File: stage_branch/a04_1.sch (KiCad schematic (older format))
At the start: 38 parts, among them U4001 74HC02, U4002 74HC27, U4003 74LVC07, U4004 74HC27, U4005 74HC02, U4006 74HC02, U4007 74HC04, U4008 74HC04, U4009 74HC27, U4010 74HC4002, U4011 74HC02, U4012 74HC02, U4013 74HC02, U4014 74HC4002, U4015 74HC27, U4016 74HC02, U4017 74HC04, U4018 74HC02, U4019 74HC02, U4020 74HC27, U4021 74HC02, U4022 74HC4002, U4023 74LVC07, U4024 74HC02, U4025 74HC04, U4026 74HC27, U4027 74HC4002, U4028 74HC4002, U4029 74LVC07, U4030 74HC02, U4058 74HC04

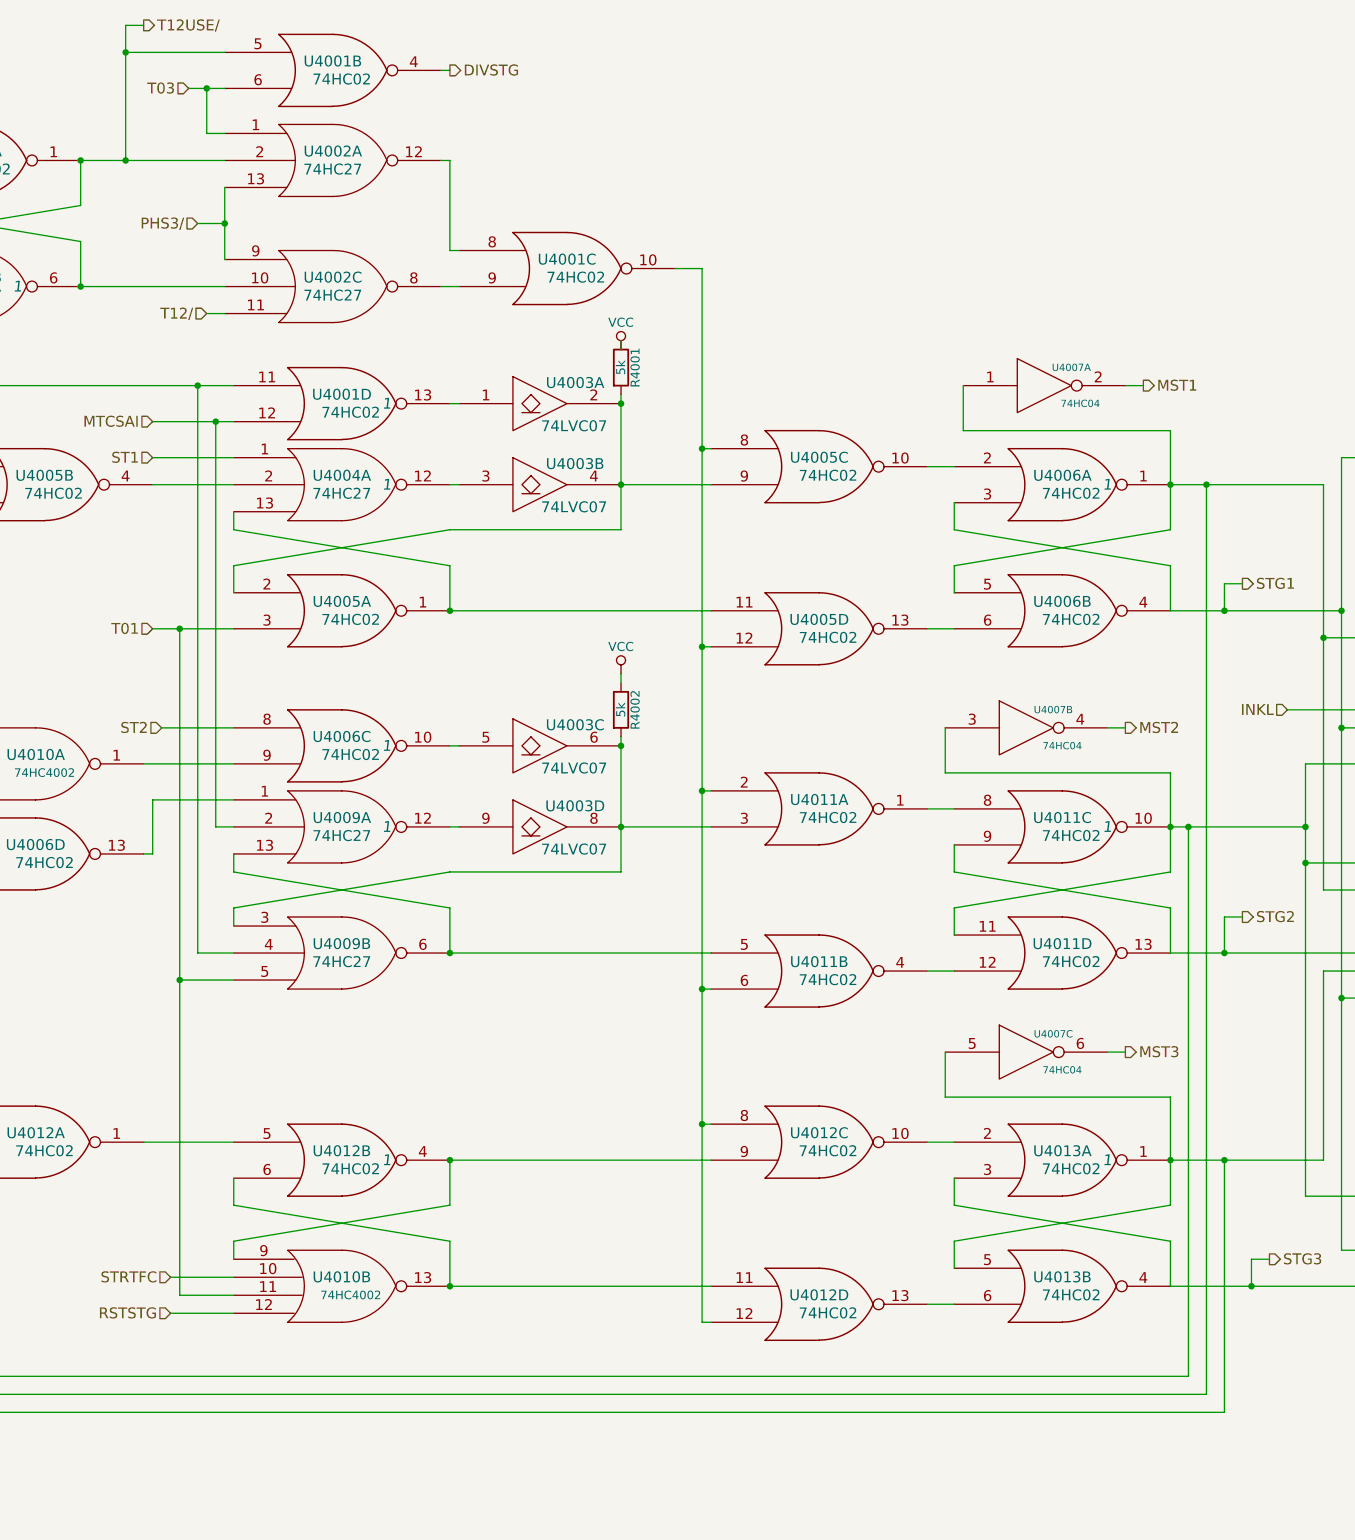
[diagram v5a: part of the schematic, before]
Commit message: Added erasable memory, and fixed lots of random wiring errors.
I decided to go with a 16-bit-wide MRAM chip -- I had  no idea
until I started researching RAM options how technologically
similar MRAM is to core memory. The datasheet diagrams look like
they're straight out of the AGC documentation!

There's a slight inaccuracy in this implementation worth mentioning.
Like fixed memory, I've wired the sense amplifier outputs directly up
to the tristate data output pins of the MRAM chip. But because the
data lines are bidirectional, data being written into RAM will show up
on the sense lines, and go straight into the ungated G register. Since
G is what's being written out, this doesn't matter 99% of the time, but
if there's an overflow condition in G (I don't even know if this is
possible), the bit 16 will be copied over bit 16, and the overflow
condition will be lost. I'll keep an eye out to see if anything relies
on G not changing after the write cycle is complete.

With erasable memory introduced, the computer now theoretically supports
all programs that don't use I/O or interrupts. I've started running
the VirtualAGC validation program, and have been fixing random errors
uncovered by failing self-tests.
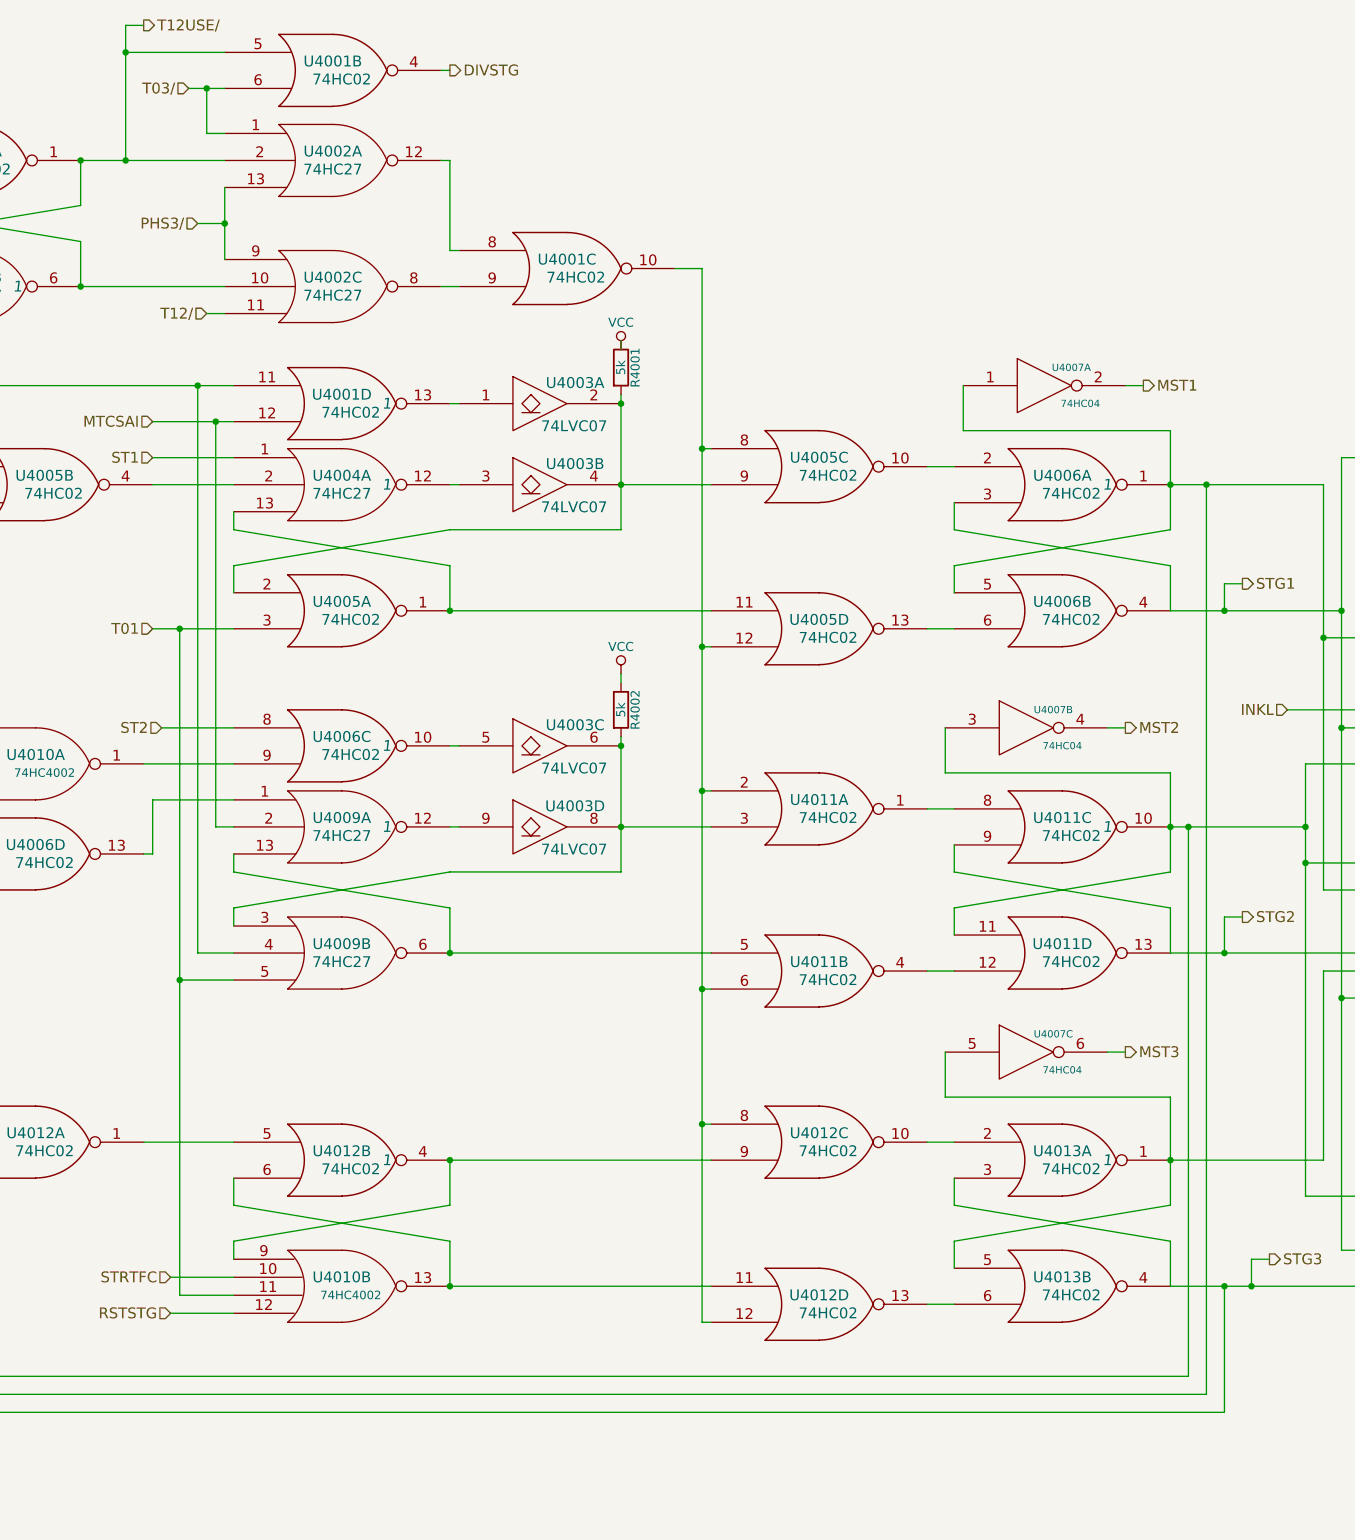
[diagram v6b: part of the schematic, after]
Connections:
- net STG3: now also U4005.6
- net at U4007.5, U4013.1, U4013.5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: no longer U4005.6
- net T03 renamed T03/
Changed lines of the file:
@@
 	900  1650 1800 1650
 Text HLabel 3600 1350 0    60   Input ~ 0
-T03
+T03/
 Wire Wire Line
 	3600 1350 3800 1350
@@
 STG3
 Wire Wire Line
-	9350 7300 9350 8700
-Wire Wire Line
 	9050 8000 10300 8000
 Wire Wire Line
@@
 Wire Wire Line
 	9900 6250 10300 6250
-Connection ~ 9350 7300
 Wire Wire Line
 	10000 6400 10300 6400
@@
 	15600 6450 15700 6450
 Connection ~ 15650 6450
+Wire Wire Line
+	9350 8000 9350 8700
+Connection ~ 9350 8000
 $EndSCHEMATC

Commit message: Added some missing net names.
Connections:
- net DVST/: now reaches U4005.5, U4006.11, U4007.12, U4012.2
- net TRSM/: now reaches U4010.2, U4058.6
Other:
- moved on the sheet: R4001, R4002, U4001A, U4001B, U4001C, U4001D, U4002A, U4002B, U4002C, U4003A, U4003B, U4003C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

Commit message: Broke all the monitor outputs I could find out to the backplane, in preparation for making a monitor
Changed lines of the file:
@@
 $EndComp
 $Comp
-L VCC #PWR06
+L VCC #PWR05
 U 1 1 56322DE9
 P 6550 2800
-F 0 "#PWR06" H 6550 2650 50  0001 C CNN
+F 0 "#PWR05" H 6550 2650 50  0001 C CNN
 F 1 "VCC" H 6550 2950 50  0000 C CNN
 F 2 "" H 6550 2800 60  0000 C CNN
@@
 $EndComp
 $Comp
-L VCC #PWR07
+L VCC #PWR06
 U 1 1 563274AD
 P 6550 4600
-F 0 "#PWR07" H 6550 4450 50  0001 C CNN
+F 0 "#PWR06" H 6550 4450 50  0001 C CNN
 F 1 "VCC" H 6550 4750 50  0000 C CNN
 F 2 "" H 6550 4600 60  0000 C CNN
@@
 	10850 3550 10750 3550
 Wire Wire Line
-	10750 8000 10750 3550
+	10750 3550 10750 8000
 $Comp
 L 74HC02 U4012
@@
 	6650 10250 6650 10200
 $Comp
-L VCC #PWR08
+L VCC #PWR07
 U 1 1 563E21C1
 P 6650 10200
-F 0 "#PWR08" H 6650 10050 50  0001 C CNN
+F 0 "#PWR07" H 6650 10050 50  0001 C CNN
 F 1 "VCC" H 6650 10350 50  0000 C CNN
 F 2 "" H 6650 10200 60  0000 C CNN
@@
 Connection ~ 9050 12150
 $Comp
-L VCC #PWR09
+L VCC #PWR08
 U 1 1 56428A57
 P 9050 11800
-F 0 "#PWR09" H 9050 11650 50  0001 C CNN
+F 0 "#PWR08" H 9050 11650 50  0001 C CNN
 F 1 "VCC" H 9050 11950 50  0000 C CNN
 F 2 "" H 9050 11800 60  0000 C CNN
@@
 $EndComp
 $Comp
-L VCC #PWR010
+L VCC #PWR09
 U 1 1 56428D13
 P 9100 12900
-F 0 "#PWR010" H 9100 12750 50  0001 C CNN
+F 0 "#PWR09" H 9100 12750 50  0001 C CNN
 F 1 "VCC" H 9100 13050 50  0000 C CNN
 F 2 "" H 9100 12900 60  0000 C CNN
@@
 Connection ~ 15750 11550
 $Comp
-L VCC #PWR011
+L VCC #PWR010
 U 1 1 5644559D
 P 15750 11200
-F 0 "#PWR011" H 15750 11050 50  0001 C CNN
+F 0 "#PWR010" H 15750 11050 50  0001 C CNN
 F 1 "VCC" H 15750 11350 50  0000 C CNN
 F 2 "" H 15750 11200 60  0000 C CNN
@@
 $EndComp
 $Comp
-L VCC #PWR012
+L VCC #PWR011
 U 1 1 56466CE0
 P 18900 11300
-F 0 "#PWR012" H 18900 11150 50  0001 C CNN
+F 0 "#PWR011" H 18900 11150 50  0001 C CNN
 F 1 "VCC" H 18900 11450 50  0000 C CNN
 F 2 "" H 18900 11300 60  0000 C CNN
